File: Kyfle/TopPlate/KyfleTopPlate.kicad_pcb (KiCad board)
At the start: 2 copper layers, 160.8 x 138.4 mm, 44 parts, among them SW2 KEY_SWITCH, SW2 PRO MICRO

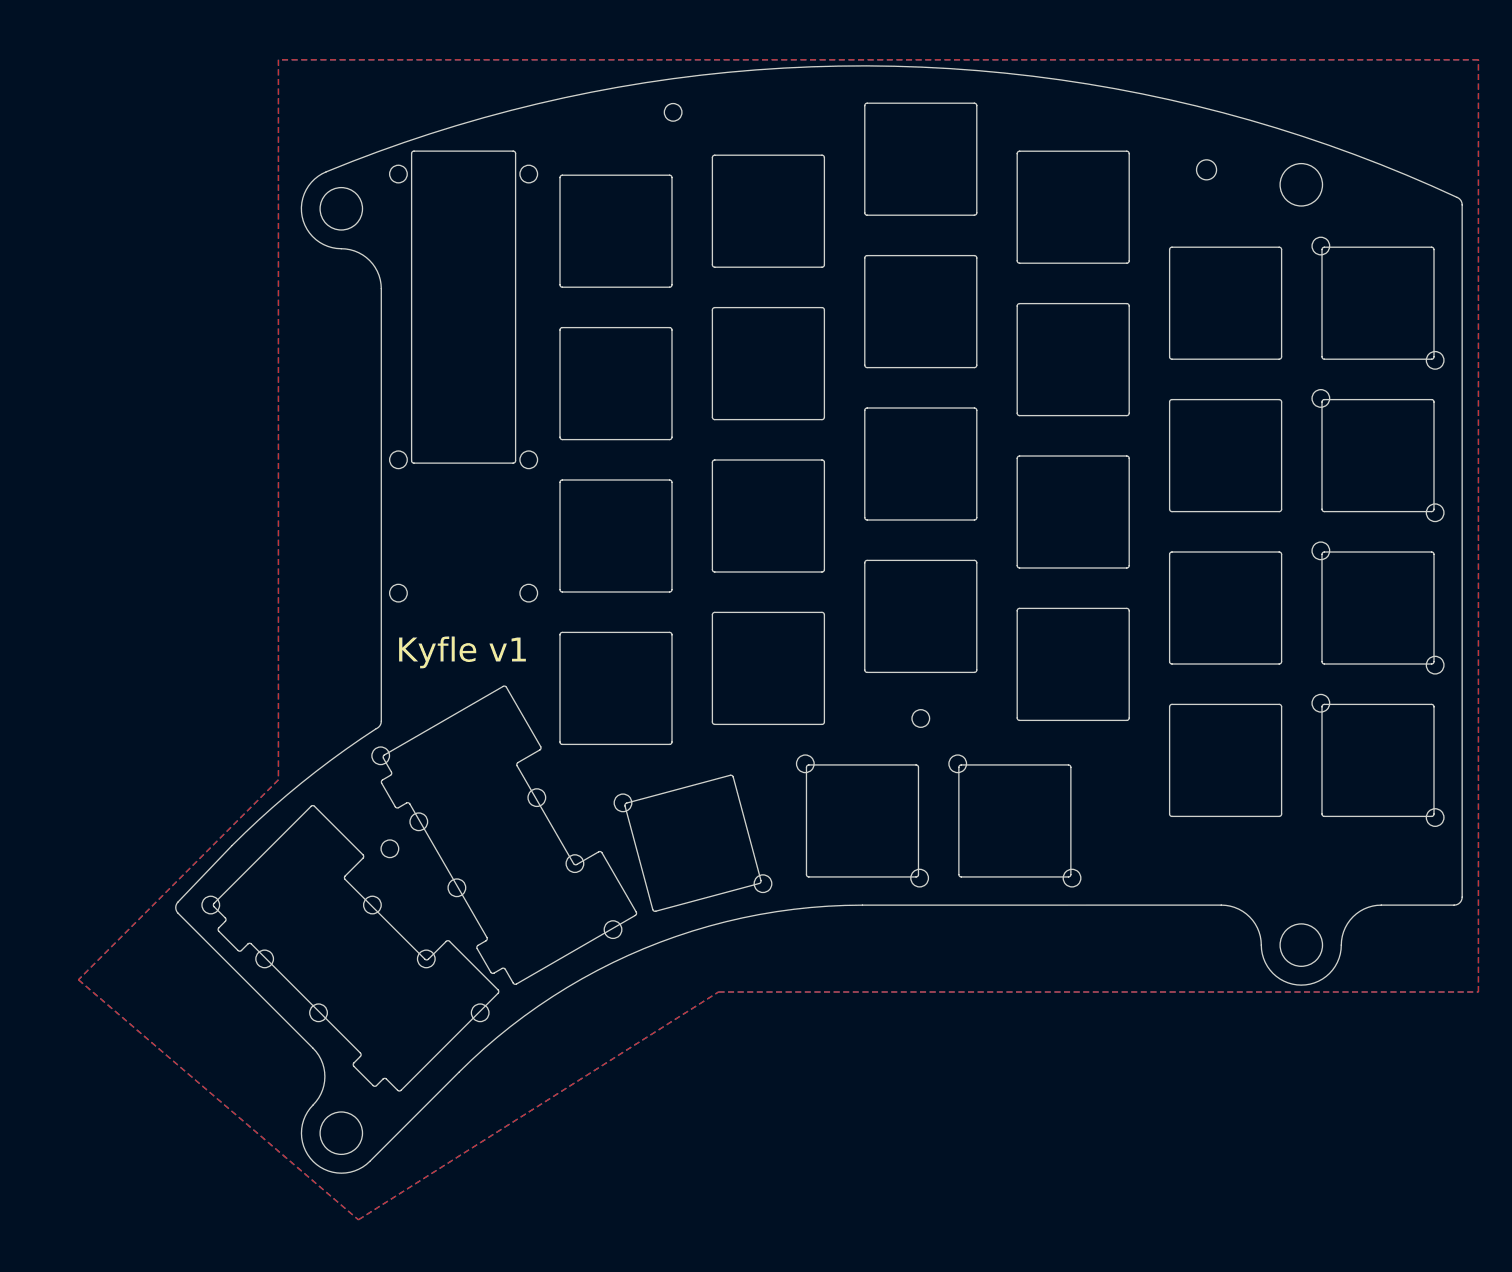
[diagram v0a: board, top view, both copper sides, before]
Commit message: Massive redesign
- Realised the design was not reversible. Only solution was to mirror the two diagonal holes of each bit. But one of them was coliding with hotswap socket footprint. Until...
- I also realised that having the holes at these Y positions made the screw coming on top collide with the bottom of the switch housing...
- So switched to having two holes right in between each bit (vertically).
- Then I realised cheap pcb houses can have quite some limitations when it comes to exotic uses of slots. In particular, for jlcpcb:
  * They prefer tabs to be >= 4mm wide
  * They prefer at least 3mm of PCB next to a slot (ie. avoid slim inter-slots parts)
  * They prefer 0.4mm clearence from board edge when it is milled/routed
  * Watching some videos of their fab it seems they do the edge.cuts routing with a single 1mm bit. Ie. if you specify a larger radius they actually route it out. And if you specify a smaller radius (than 0.5mm) they cannot do it.

So, I redid the PCB. Twice... Again. For now...

I also started reorganising the projects. First part was to gather all footprints used accross the three boards. Makes cross-board editing of footprints easier.
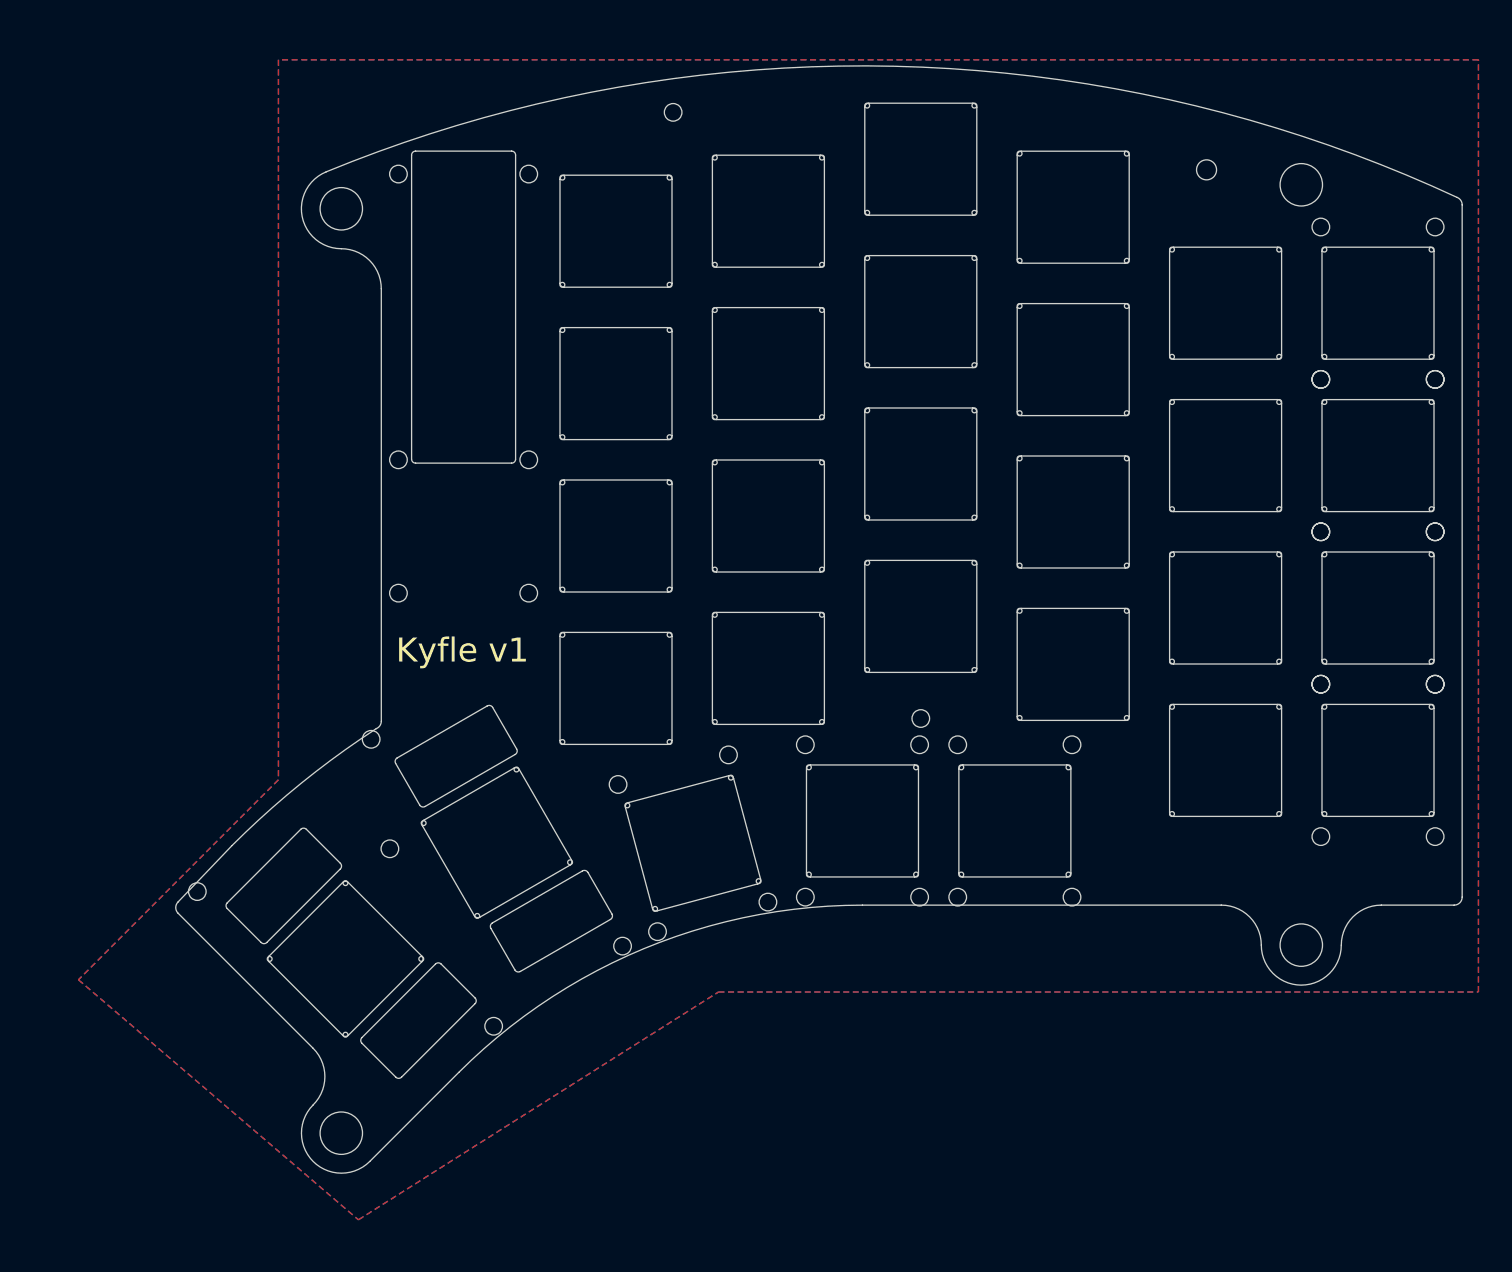
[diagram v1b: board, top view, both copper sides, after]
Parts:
- REF** (x4): footprint SofleChocTop:M5_with_washer -> Kyfle Footprints:M5_with_washer
- REF** (x6), TH3, TH7 (x2): footprint SofleChocTop:M2_with_washer -> Kyfle Footprints:M2_with_washer
- SW2: footprint SofleChocTop:SU120_ProMicro_Top -> Kyfle Footprints:Arduino_ProMicro_Kyfle_v1_TopPlate
- SW2 (x7): footprint SofleChocTop:SU120_RGB_SW_Top_drilled -> Kyfle Footprints:CherryMX_Kyfle_v1_TopPlate_1u_Drilled
- SW2 (x20): footprint SofleChocTop:SU120_RGB_SW_Top -> Kyfle Footprints:CherryMX_Kyfle_v1_TopPlate_1u
- SW2 (x2): footprint SofleChocTop:SU120_RGB_SW_2u_Top -> Kyfle Footprints:CherryMX_Kyfle_v1_TopPlate_2u
- SW2: footprint SofleChocTop:SK6812_Bit -> Kyfle Footprints:SK6812_Bit
- turned SW2 to 210 degrees
- turned SW2 to 225 degrees

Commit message: PCB done. Started redoing the rails.
- PCB should be in its final version now, pretty much. I hope...
- I added a tentative compatibility with Panasonic roller encoders.
- Also added some silk screens for the 2u stabilisers.
- Propagated the new bit board design to footprints used for top and bottom plate.
- And started to rework the rails in the bottom plate, as well as the general shape of the keyboard.
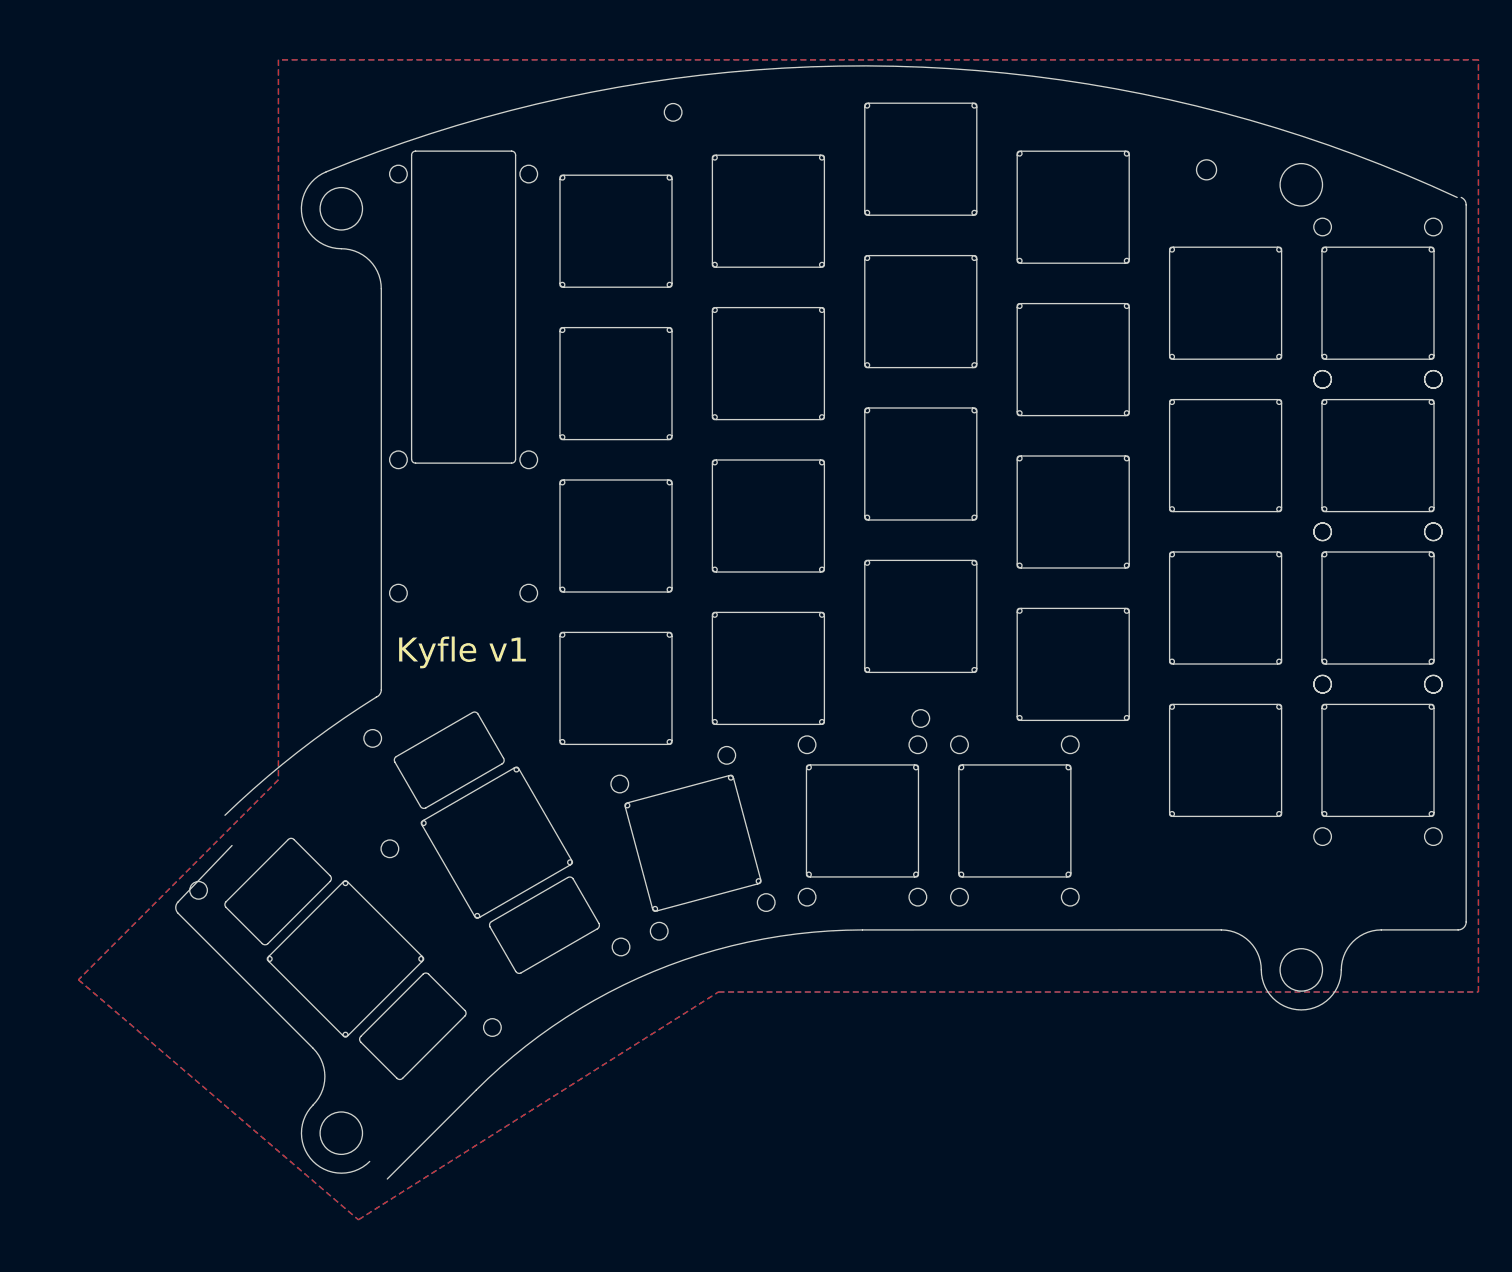
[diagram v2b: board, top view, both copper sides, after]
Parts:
- moved REF** 3.10 mm to (216.6, 136.7)
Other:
- board size 160.8 x 138.4 mm -> 161.3 x 139.1 mm

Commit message: Plates outlines finished
Redefined the various outlines of the plates based on the new constrains.
For the top dimension, I took the largest middle-finger stagerring I could find (Elephant42, at +9.5mm) and rounded it to 10mm max amplitude in the middle finger rail, and used that as reference for the position of the top arc (giving 3mm margin above that highest slot).
And defined the position of the rest from that.
Top left M% hole might need to be reviewed.
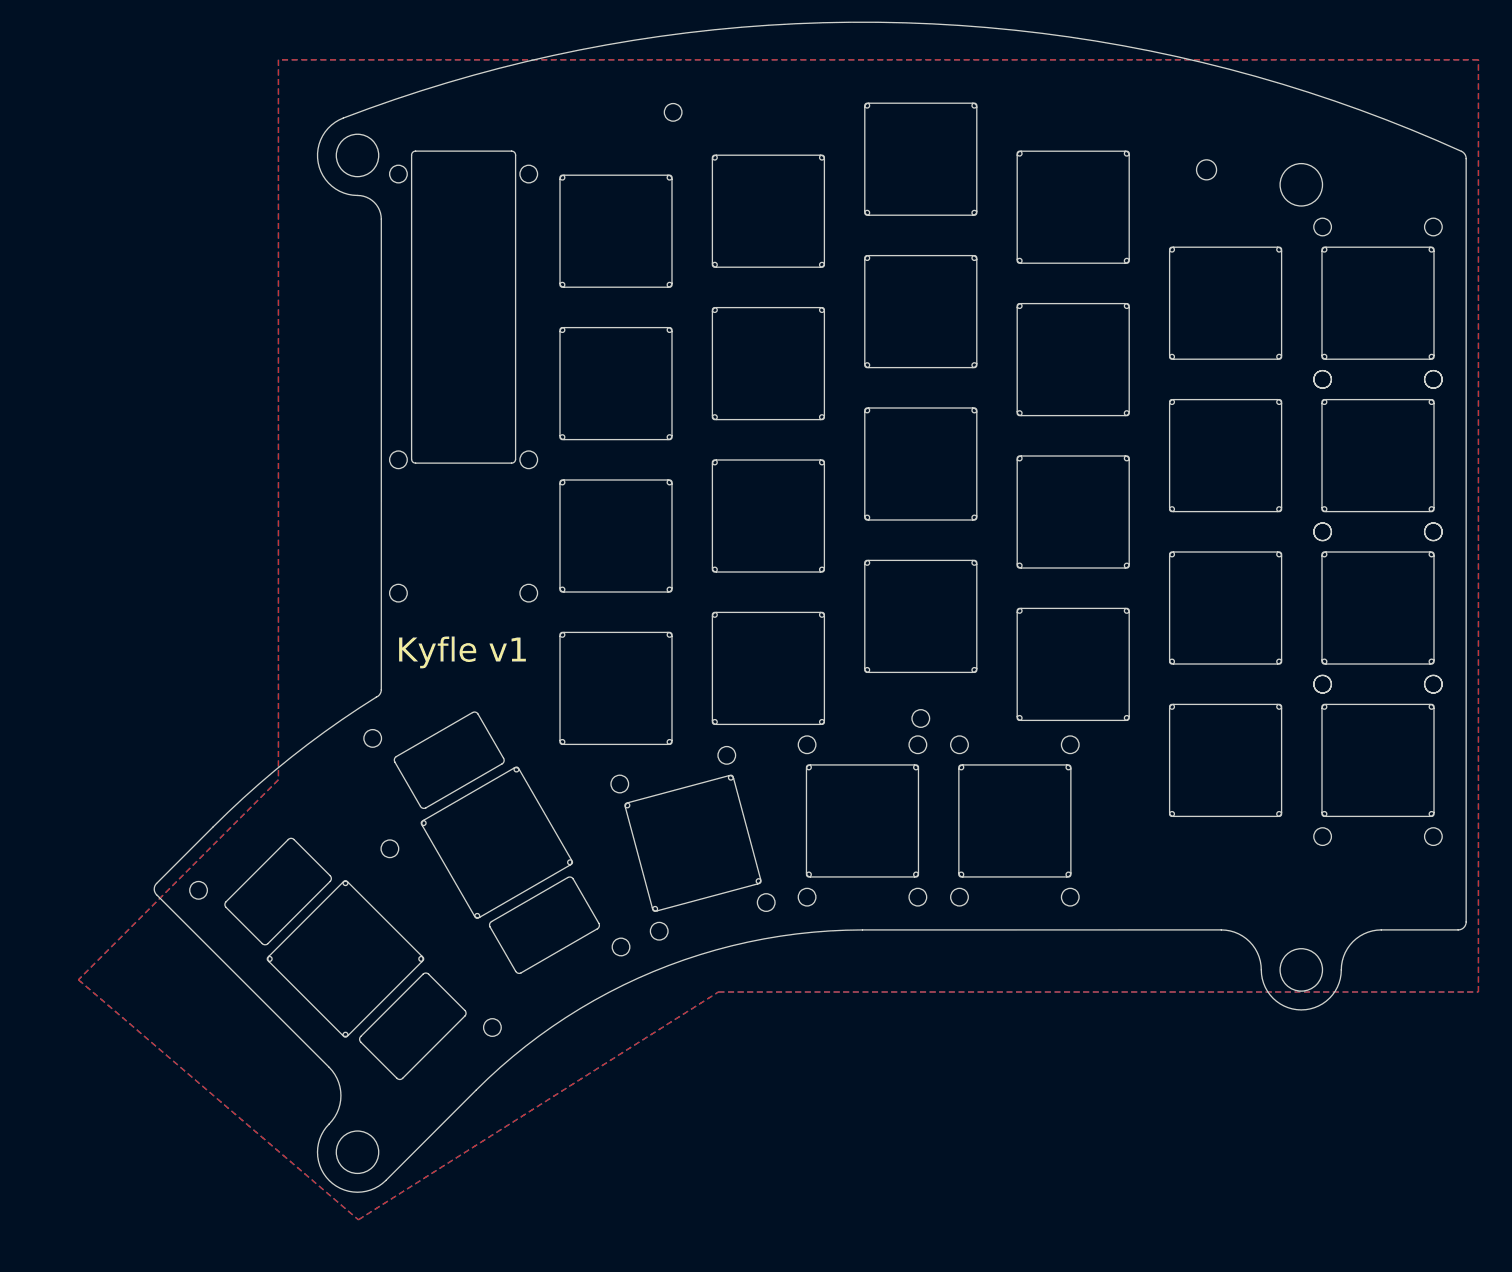
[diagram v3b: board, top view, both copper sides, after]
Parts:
- REF**: footprint Kyfle Footprints:M5_with_washer -> Kyfle Footprints:M5_with_washer_and_board
- moved REF** 8.12 mm to (102.2, 163.1), turned to 315 degrees
- moved REF** 6.97 mm to (98.6, 34.9)
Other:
- board size 161.3 x 139.1 mm -> 164 x 146.2 mm

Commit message: Touch ups and small works
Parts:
- REF**: footprint Kyfle Footprints:M5_with_washer -> Kyfle Footprints:M5_with_washer_and_board
- SW2 (x2): footprint Kyfle Footprints:CherryMX_Kyfle_v1_TopPlate_2u -> Kyfle Footprints:CherryMX_Kyfle_v1_TopPlate_2u_1u
- moved REF** 20.6 mm to (237.2, 136.7)
- moved REF** 15.6 mm to (232.2, 37.9)
- moved TH3 12.1 mm to (150.0, 27.4)
- moved TH7 7.81 mm to (97.3, 116.0)
- moved TH7 1.26 mm to (169.1, 104.0)
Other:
- board size 164 x 146.2 mm -> 164 x 146.3 mm
